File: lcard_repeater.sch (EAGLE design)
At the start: 71 parts, among them X1 236-741-5,08, X10 236-741-5,08, X11 236-741-5,08, X12 236-741-5,08, X13 236-741-5,08, X14 236-741-5,08, X15 236-741-5,08, X16 236-741-5,08, X17 236-741-5,08, X18 236-741-5,08, X19 236-741-5,08, X20 236-741-5,08, X21 236-741-5,08, X22 236-741-5,08, X23 236-741-5,08, X24 236-741-5,08, X25 236-741-5,08, X3 236-741-5,08, X4 236-741-5,08, X5 236-741-5,08, X6 236-741-5,08, X7 236-741-5,08, X8 236-741-5,08, X9 236-741-5,08

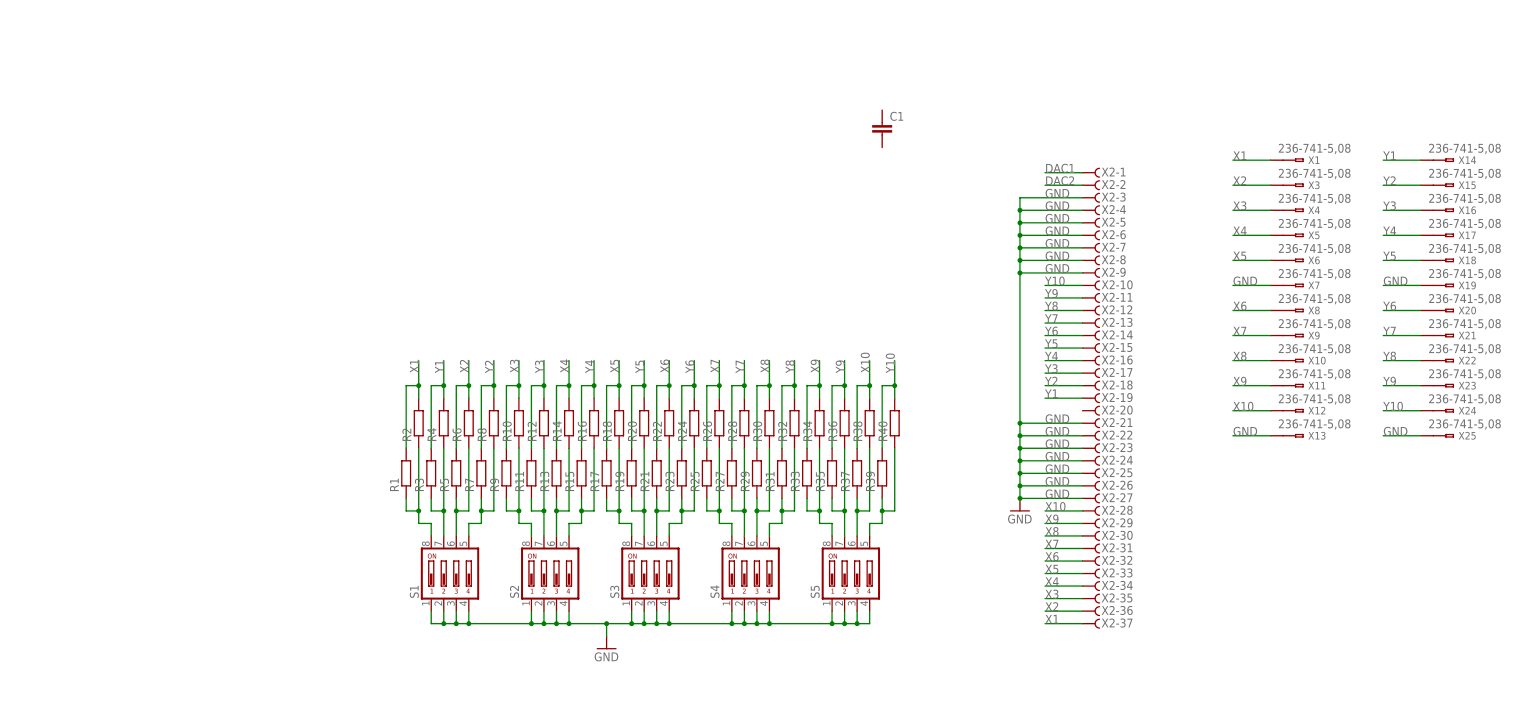
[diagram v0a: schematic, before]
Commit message: Доделана схема и расставлены элементы на плате
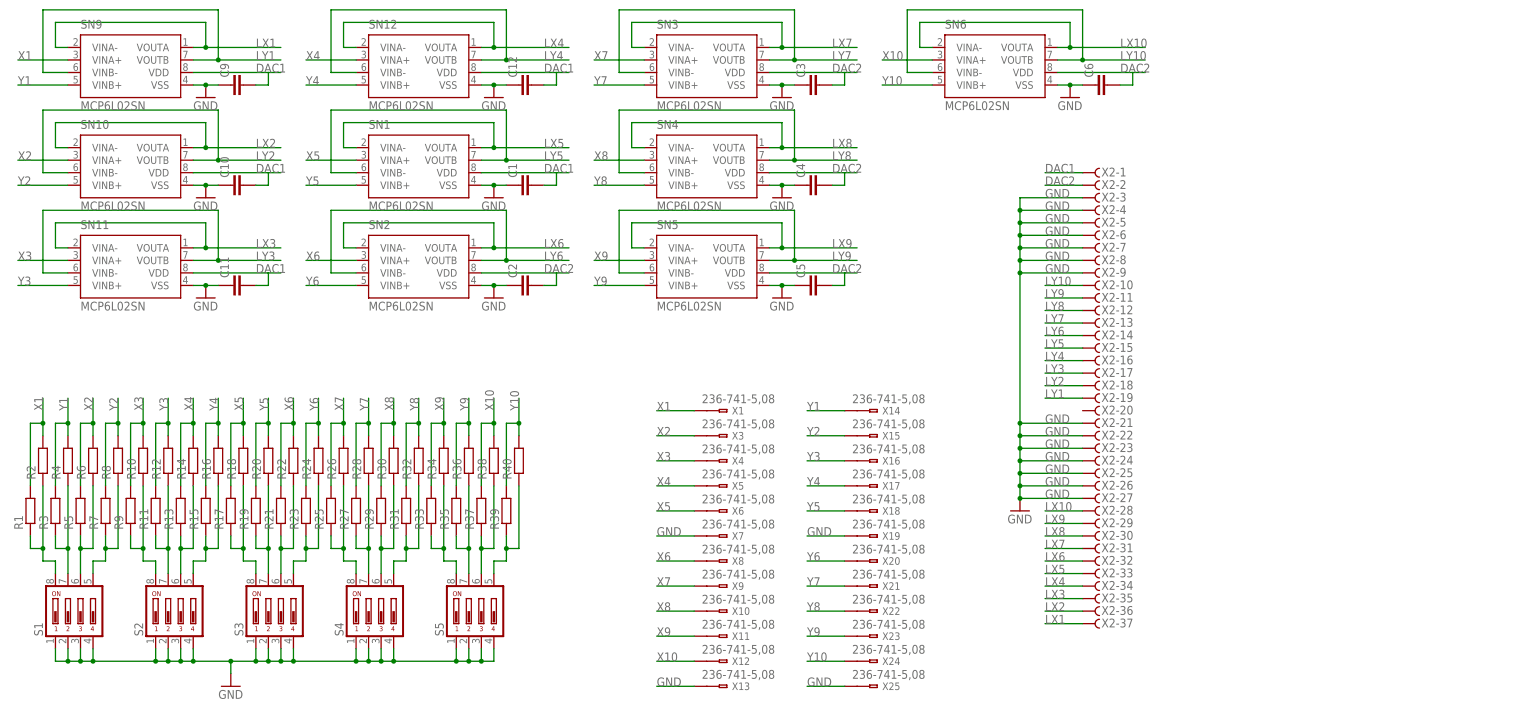
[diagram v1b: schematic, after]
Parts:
- added C10, C11, C12, C2, C3, C4, C5, C6, C9: (no value), lcard_repeater:C-EUC1206
- added SN1, SN10, SN11, SN12, SN2, SN3, SN4, SN5, SN6, SN9: MCP6L02SN, lcard_repeater:MCP6L02SN
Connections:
- new net LX1: SN9.VINA-, SN9.VOUTA, X2-37.F
- new net LX10: SN6.VINA-, SN6.VOUTA, X2-28.F
- new net LX2: SN10.VINA-, SN10.VOUTA, X2-36.F
- new net LX3: SN11.VINA-, SN11.VOUTA, X2-35.F
- new net LX4: SN12.VINA-, SN12.VOUTA, X2-34.F
- new net LX5: SN1.VINA-, SN1.VOUTA, X2-33.F
- new net LX6: SN2.VINA-, SN2.VOUTA, X2-32.F
- new net LX7: SN3.VINA-, SN3.VOUTA, X2-31.F
- new net LX8: SN4.VINA-, SN4.VOUTA, X2-30.F
- new net LX9: SN5.VINA-, SN5.VOUTA, X2-29.F
- new net LY1: SN9.VINB-, SN9.VOUTB, X2-19.F
- new net LY10: SN6.VINB-, SN6.VOUTB, X2-10.F
- new net LY2: SN10.VINB-, SN10.VOUTB, X2-18.F
- new net LY3: SN11.VINB-, SN11.VOUTB, X2-17.F
- new net LY4: SN12.VINB-, SN12.VOUTB, X2-16.F
- new net LY5: SN1.VINB-, SN1.VOUTB, X2-15.F
- new net LY6: SN2.VINB-, SN2.VOUTB, X2-14.F
- new net LY7: SN3.VINB-, SN3.VOUTB, X2-13.F
- new net LY8: SN4.VINB-, SN4.VOUTB, X2-12.F
- new net LY9: SN5.VINB-, SN5.VOUTB, X2-11.F
- net DAC1: now also C1.2, C10.2, C11.2, C12.2, C9.2, SN1.VDD, SN10.VDD, SN11.VDD, SN12.VDD, SN9.VDD
- net DAC2: now also C2.2, C3.2, C4.2, C5.2, C6.2, SN2.VDD, SN3.VDD, SN4.VDD, SN5.VDD, SN6.VDD
- net GND: now also C1.1, C10.1, C11.1, C12.1, C2.1, C3.1, C4.1, C5.1, C6.1, C9.1, SN1.VSS, SN10.VSS, SN11.VSS, SN12.VSS, SN2.VSS, SN3.VSS, SN4.VSS, SN5.VSS, SN6.VSS, SN9.VSS
- net X1: now also SN9.VINA+; no longer X2-37.F
- net X10: now also SN6.VINA+
- net X2: now also SN10.VINA+; no longer X2-36.F
- net X3: now also SN11.VINA+
- net X4: now also SN12.VINA+
- net X5: now also SN1.VINA+
- net X6: now also SN2.VINA+
- net X7: now also SN3.VINA+
- net X8: now also SN4.VINA+
- net X9: now also SN5.VINA+
- net Y1: now also SN9.VINB+; no longer X2-19.F
- net Y10: now also SN6.VINB+
- net Y2: now also SN10.VINB+
- net Y3: now also SN11.VINB+
- net Y4: now also SN12.VINB+
- net Y5: now also SN1.VINB+
- net Y6: now also SN2.VINB+
- net Y7: now also SN3.VINB+
- net Y8: now also SN4.VINB+
- net Y9: now also SN5.VINB+
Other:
- moved on the sheet: C1, R1, R10, R11, R12, R13, R14, R15, R16, R17, R18, R19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
